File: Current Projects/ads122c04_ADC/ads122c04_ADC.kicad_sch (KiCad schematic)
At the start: 23 parts, among them J1 Conn_01x05, J2 Conn_01x04, U1 ADS122C04IPWR, U2 MCP1711T-33I/OT

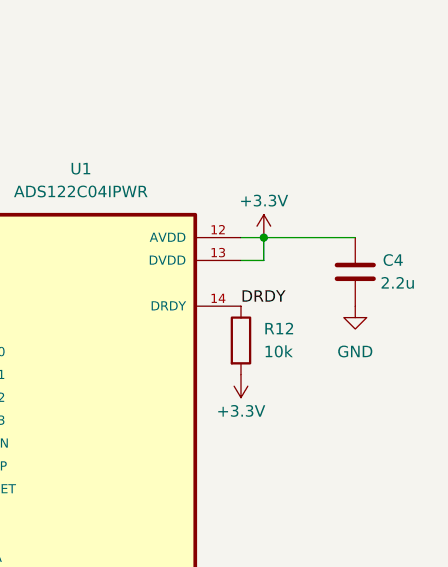
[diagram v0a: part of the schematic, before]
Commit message: Added BOM to project. See the csv file.
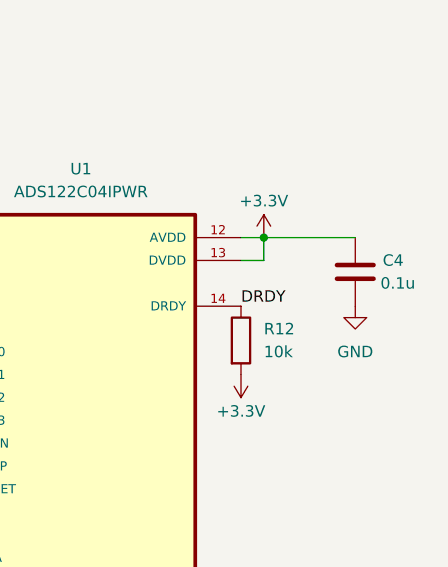
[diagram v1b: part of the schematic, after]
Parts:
- C4: value 2.2u -> 0.1u
- R1, R2, R3, R4, R5, R6, R7, R8: now left out of the parts list
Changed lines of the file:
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@@
 			)
 		)
-		(property "Value" "2.2u"
+		(property "Value" "0.1u"
 			(at 195.834 76.2 0)
 			(effects
@@
 		(unit 1)
 		(exclude_from_sim no)
-		(in_bom yes)
+		(in_bom no)
 		(on_board yes)
 		(dnp no)
@@
 		(unit 1)
 		(exclude_from_sim no)
-		(in_bom yes)
+		(in_bom no)
 		(on_board yes)
 		(dnp no)
@@
 		(unit 1)
 		(exclude_from_sim no)
-		(in_bom yes)
+		(in_bom no)
 		(on_board yes)
 		(dnp no)
@@
 		(unit 1)
 		(exclude_from_sim no)
-		(in_bom yes)
+		(in_bom no)
 		(on_board yes)
 		(dnp no)
@@
 		(unit 1)
 		(exclude_from_sim no)
-		(in_bom yes)
+		(in_bom no)
 		(on_board yes)
 		(dnp no)
@@
 		(unit 1)
 		(exclude_from_sim no)
-		(in_bom yes)
+		(in_bom no)
 		(on_board yes)
 		(dnp no)
@@
 		(unit 1)
 		(exclude_from_sim no)
-		(in_bom yes)
+		(in_bom no)
 		(on_board yes)
 		(dnp no)
@@
 		(unit 1)
 		(exclude_from_sim no)
-		(in_bom yes)
-		(on_board yes)
-		(dnp no)
+		(in_bom no)
+		(on_board yes)
+		(dnp no)

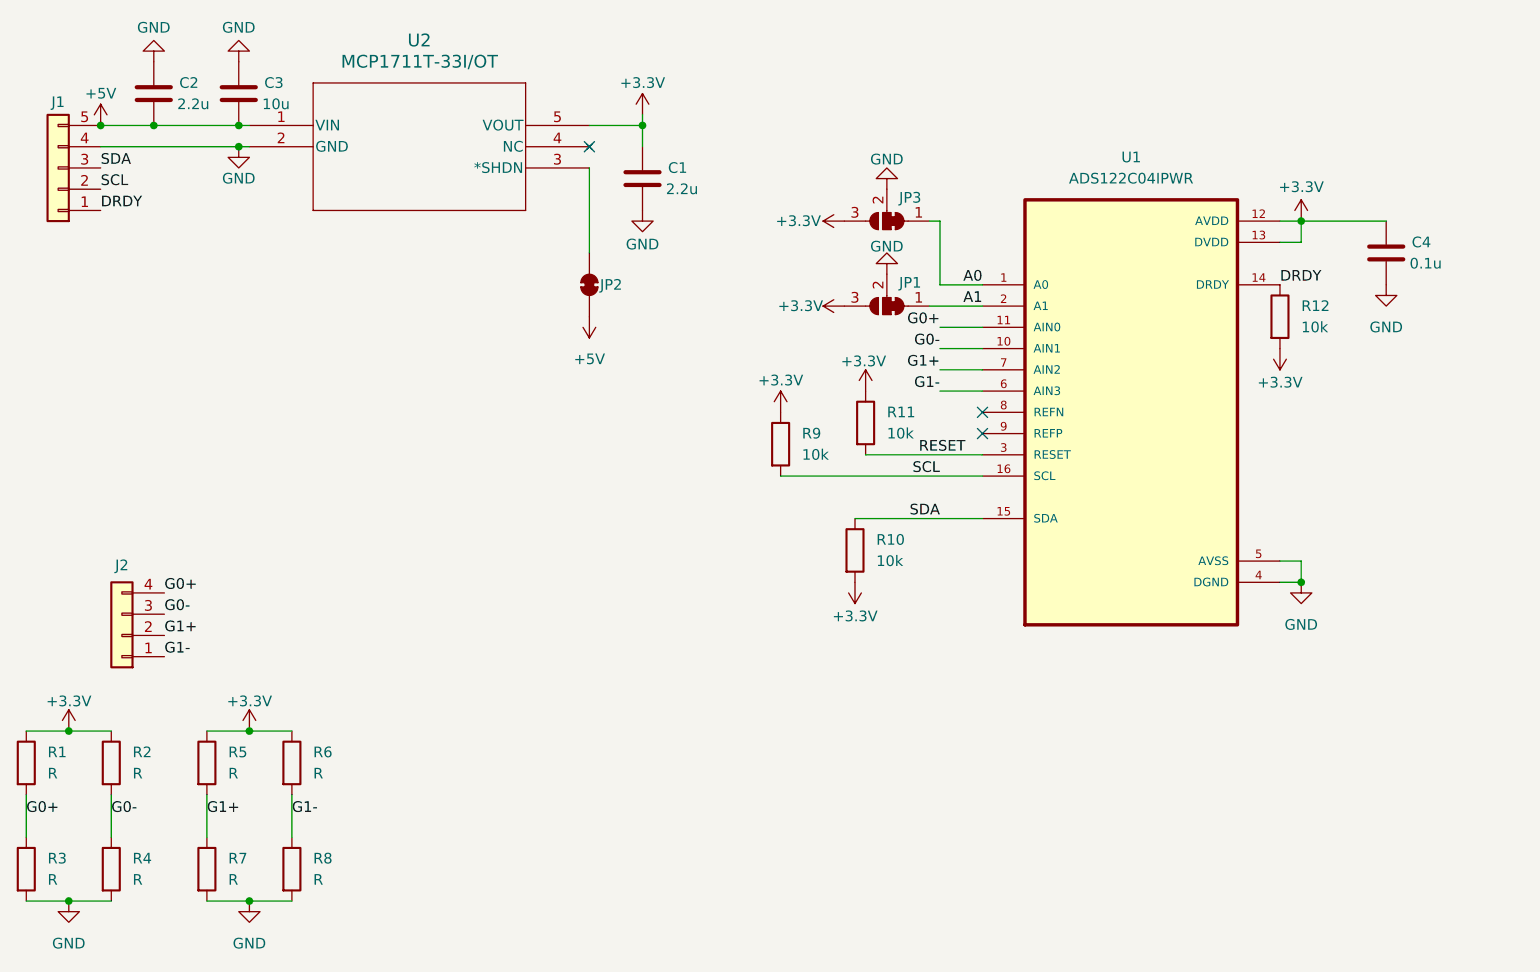
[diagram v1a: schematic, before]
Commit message: Increased trace widths, added silkscreen doodle, adding proper filtering caps for power signals, increased board size to 2x1.1, and swapped voltage regulator with proper one.
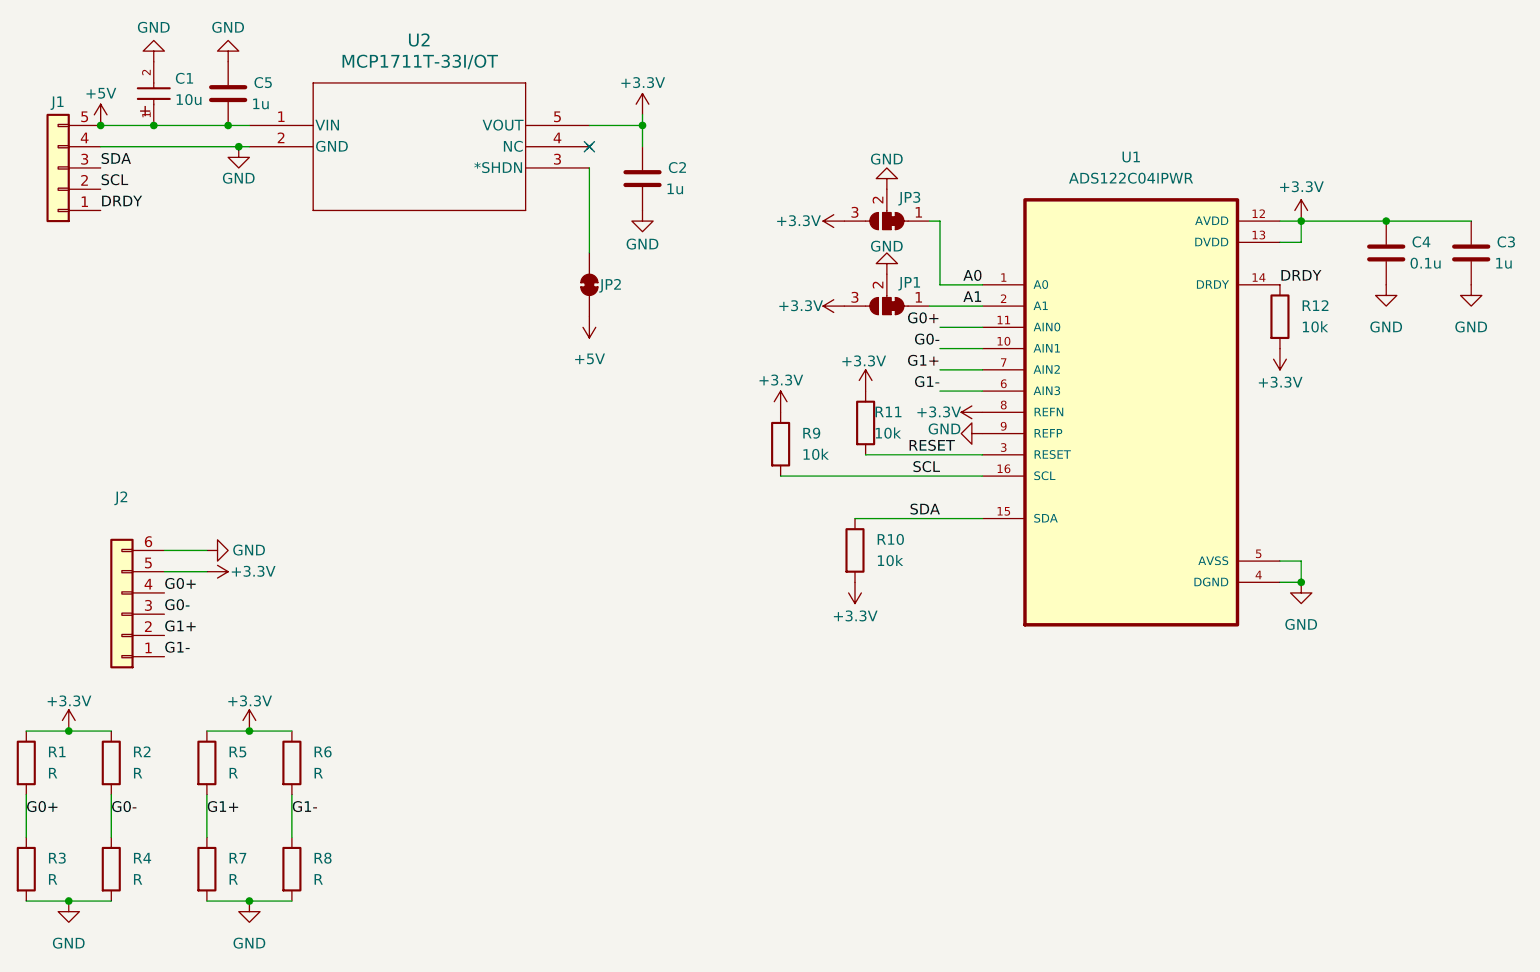
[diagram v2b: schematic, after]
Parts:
- removed C2: 2.2u, Capacitor_SMD:C_0805_2012Metric_Pad1.18x1.45mm_HandSolder, symbol Device:C
- removed J2: Conn_01x04, Connector_PinHeader_2.54mm:PinHeader_1x04_P2.54mm_Vertical, symbol Connector_Generic:Conn_01x04
- added C1: 10u, 865080340001:WCAP-ASLI_4X5.5_DXL_, symbol WCAP-ASLI_4X5.5:WCAP-ASLI_4X5.5
- added C5: 1u, Capacitor_SMD:C_0805_2012Metric_Pad1.18x1.45mm_HandSolder, symbol Device:C
- added J2: Conn_01x06, Connector_PinHeader_2.54mm:PinHeader_1x06_P2.54mm_Vertical, symbol Connector_Generic:Conn_01x06
- C2: renamed from C1; value 2.2u -> 1u
- C3: value 10u -> 1u
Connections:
- net +3.3V: now also C3.1, U1.8 (REFN), J2.5 (Pin_5)
- net +5V: now also C1.1, C5.2; no longer C3.2
- net G0+: now also J2.4 (Pin_4)
- net G0-: now also J2.3 (Pin_3)
- net G1+: now also J2.2 (Pin_2)
- net G1-: now also J2.1 (Pin_1)
- net GND: now also C3.2, U1.9 (REFP), C1.2, C5.1, J2.6 (Pin_6); no longer C3.1
- no-connect marks 3 -> 1

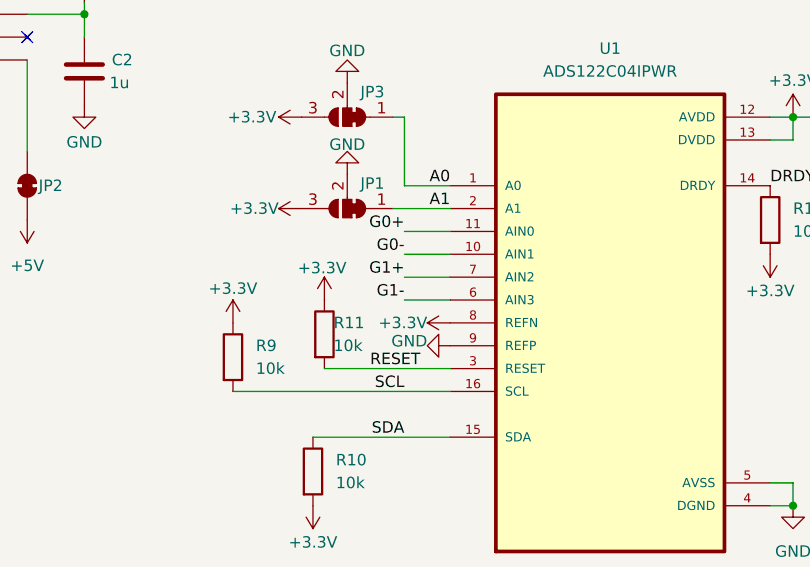
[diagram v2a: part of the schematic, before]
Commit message: Added gerbers for ordering. Fixed issues with the reference voltage.
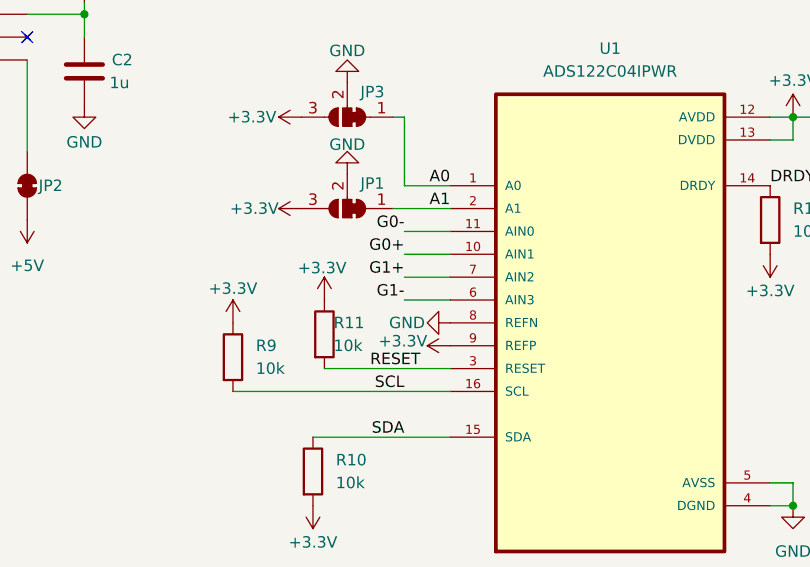
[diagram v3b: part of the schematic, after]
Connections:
- net +3.3V: now also U1.9 (REFP); no longer U1.8 (REFN)
- net G0+: now also U1.10 (AIN1); no longer U1.11 (AIN0)
- net G0-: now also U1.11 (AIN0); no longer U1.10 (AIN1)
- net GND: now also U1.8 (REFN); no longer U1.9 (REFP)
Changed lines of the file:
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@@
 	(wire
 		(pts
-			(xy 30.48 152.4) (xy 35.56 152.4)
+			(xy 139.7 86.36) (xy 144.78 86.36)
 		)
 		(stroke
@@
 	(wire
 		(pts
-			(xy 62.23 139.7) (xy 62.23 144.78)
+			(xy 30.48 152.4) (xy 35.56 152.4)
 		)
 		(stroke
@@
 	(wire
 		(pts
-			(xy 30.48 132.08) (xy 35.56 132.08)
+			(xy 62.23 139.7) (xy 62.23 144.78)
 		)
 		(stroke
@@
 	(wire
 		(pts
-			(xy 139.7 88.9) (xy 144.78 88.9)
+			(xy 30.48 132.08) (xy 35.56 132.08)
 		)
 		(stroke
@@
 	(wire
 		(pts
-			(xy 182.88 114.3) (xy 180.34 114.3)
+			(xy 139.7 88.9) (xy 144.78 88.9)
 		)
 		(stroke
@@
 	(wire
 		(pts
-			(xy 180.34 73.66) (xy 182.88 73.66)
+			(xy 182.88 114.3) (xy 180.34 114.3)
 		)
 		(stroke
@@
 	(wire
 		(pts
-			(xy 139.7 83.82) (xy 144.78 83.82)
+			(xy 180.34 73.66) (xy 182.88 73.66)
 		)
 		(stroke
@@
 	(wire
 		(pts
-			(xy 139.7 86.36) (xy 144.78 86.36)
+			(xy 57.15 152.4) (xy 62.23 152.4)
 		)
 		(stroke
@@
 	(wire
 		(pts
-			(xy 57.15 152.4) (xy 62.23 152.4)
+			(xy 35.56 132.08) (xy 40.64 132.08)
 		)
 		(stroke
@@
 	(wire
 		(pts
-			(xy 35.56 132.08) (xy 40.64 132.08)
+			(xy 52.07 110.49) (xy 46.99 110.49)
 		)
 		(stroke
@@
 	(wire
 		(pts
-			(xy 52.07 110.49) (xy 46.99 110.49)
+			(xy 139.7 91.44) (xy 144.78 91.44)
 		)
 		(stroke
@@
 	(wire
 		(pts
-			(xy 139.7 91.44) (xy 144.78 91.44)
+			(xy 182.88 111.76) (xy 182.88 114.3)
 		)
 		(stroke
@@
 	(wire
 		(pts
-			(xy 182.88 111.76) (xy 182.88 114.3)
+			(xy 139.7 83.82) (xy 144.78 83.82)
 		)
 		(stroke
@@
 	)
 	(label "G0-"
-		(at 139.7 86.36 180)
+		(at 139.7 83.82 180)
 		(effects
 			(font
@@
 	)
 	(label "G0+"
-		(at 139.7 83.82 180)
+		(at 139.7 86.36 180)
 		(effects
 			(font
@@
 	(symbol
 		(lib_id "power:+3.3V")
-		(at 144.78 93.98 90)
+		(at 144.78 96.52 90)
 		(unit 1)
 		(exclude_from_sim no)
@@
 		(dnp no)
 		(property "Reference" "#PWR023"
-			(at 148.59 93.98 0)
+			(at 148.59 96.52 0)
 			(effects
 				(font
@@
 		)
 		(property "Value" "+3.3V"
-			(at 142.24 93.98 90)
+			(at 142.24 96.012 90)
 			(effects
 				(font
@@
 		)
 		(property "Footprint" ""
-			(at 144.78 93.98 0)
+			(at 144.78 96.52 0)
 			(effects
 				(font
@@
 		)
 		(property "Datasheet" ""
-			(at 144.78 93.98 0)
+			(at 144.78 96.52 0)
 			(effects
 				(font
@@
 		)
 		(property "Description" "Power symbol creates a global label with name \"+3.3V\""
-			(at 144.78 93.98 0)
+			(at 144.78 96.52 0)
 			(effects
 				(font
@@
 	(symbol
 		(lib_id "power:GND")
-		(at 144.78 96.52 270)
+		(at 144.78 93.98 270)
 		(unit 1)
 		(exclude_from_sim no)
@@
 		(dnp no)
 		(property "Reference" "#PWR024"
-			(at 138.43 96.52 0)
+			(at 138.43 93.98 0)
 			(effects
 				(font
@@
 		)
 		(property "Value" "GND"
-			(at 142.24 96.012 90)
+			(at 141.986 93.98 90)
 			(effects
 				(font
@@
 		)
 		(property "Footprint" ""
-			(at 144.78 96.52 0)
+			(at 144.78 93.98 0)
 			(effects
 				(font
@@
 		)
 		(property "Datasheet" ""
-			(at 144.78 96.52 0)
+			(at 144.78 93.98 0)
 			(effects
 				(font
@@
 		)
 		(property "Description" "Power symbol creates a global label with name \"GND\" , ground"
-			(at 144.78 96.52 0)
+			(at 144.78 93.98 0)
 			(effects
 				(font
